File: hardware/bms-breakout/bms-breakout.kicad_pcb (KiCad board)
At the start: 2 copper layers, 116.5 x 125.3 mm, 32 parts, among them J1 IN-A, J10 V-SUPP, J11 Smol_Brain_Board, J13 UART_CONN, J16 ESTOP_CON, J17 I2C_Conn, J18 BAL_3, J19 BAL_2, J2 IN-B, J20 BAL_1, J21 DE9_Socket_MountingHoles, J22 DE9_Socket_MountingHoles, J23 FAN-IN, J24 SWITCH, J3 IN-C, J4 BALANCE-A, J5 BALANCE-B, J6 BALANCE-C, J7 Conn_01x02, Q1 PMOZZ, SW1 Kill_Switch

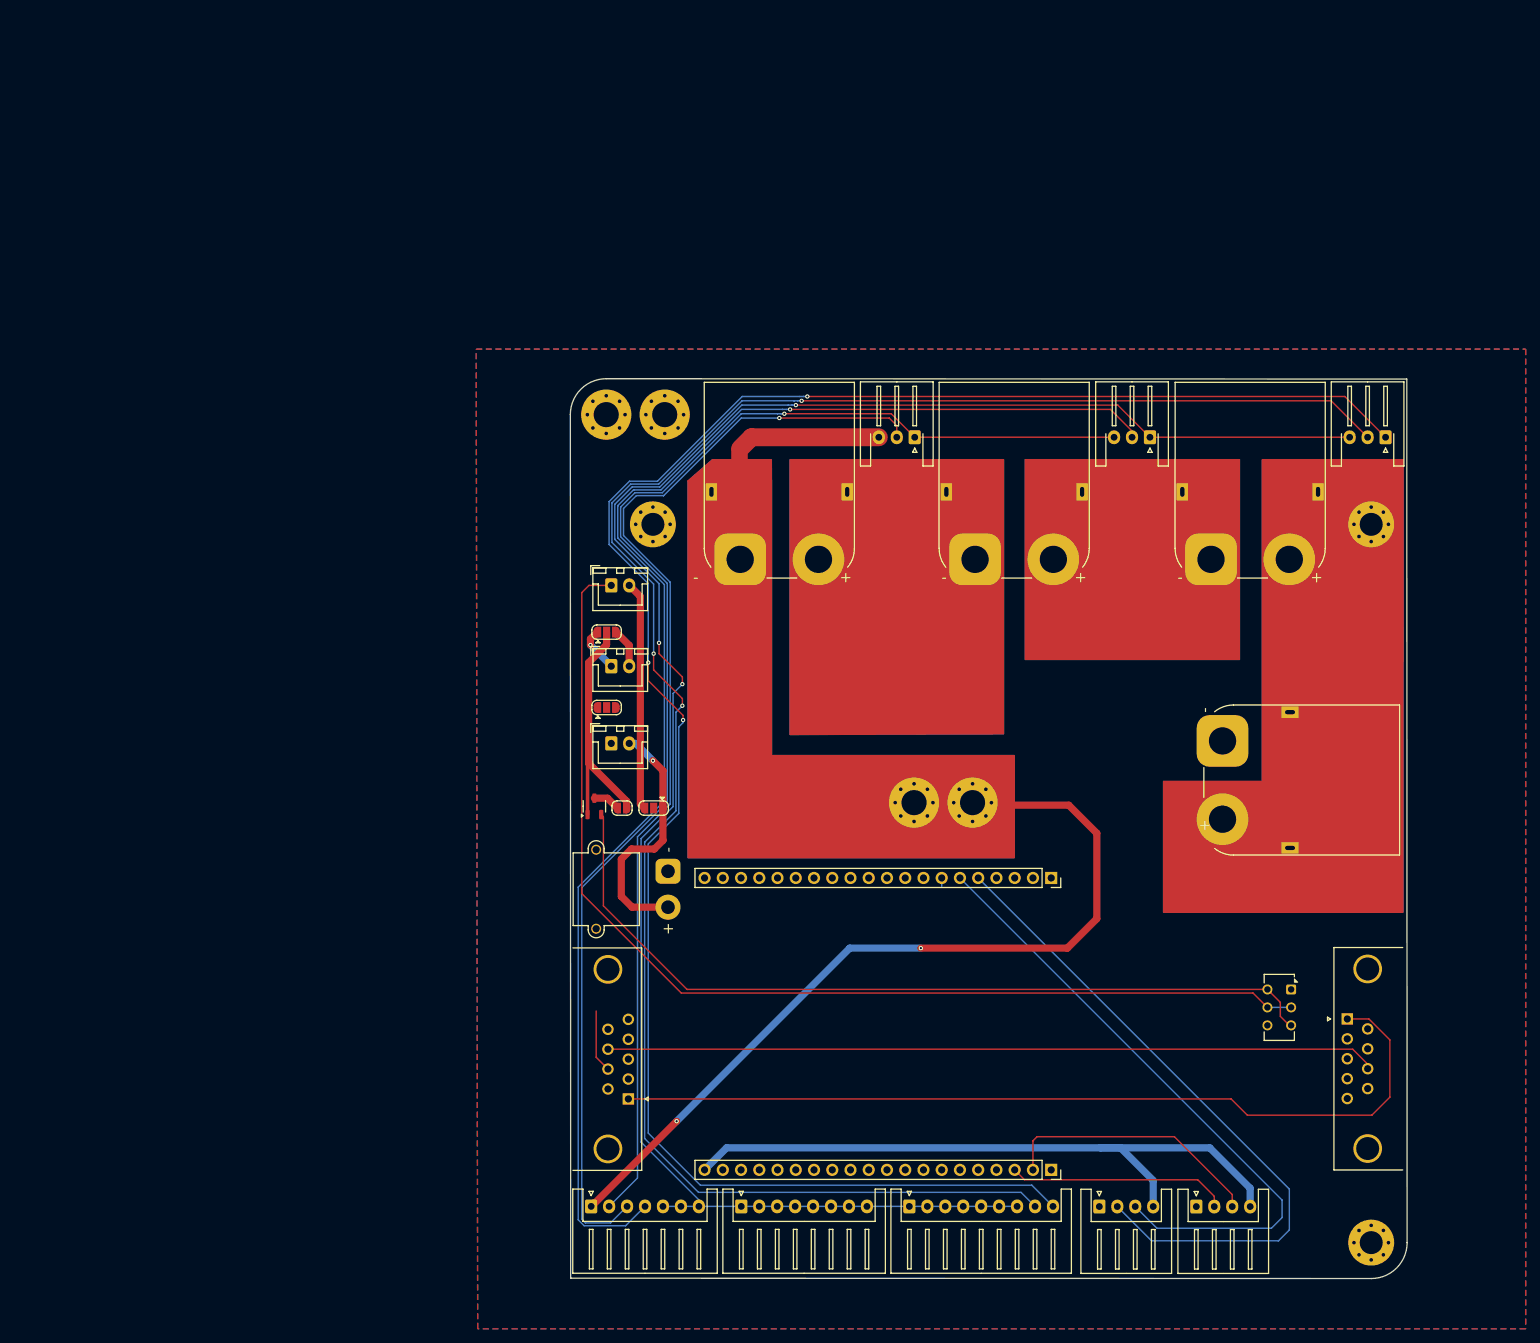
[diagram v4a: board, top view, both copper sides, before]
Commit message: Final Touches
- Added graphics
- Added text
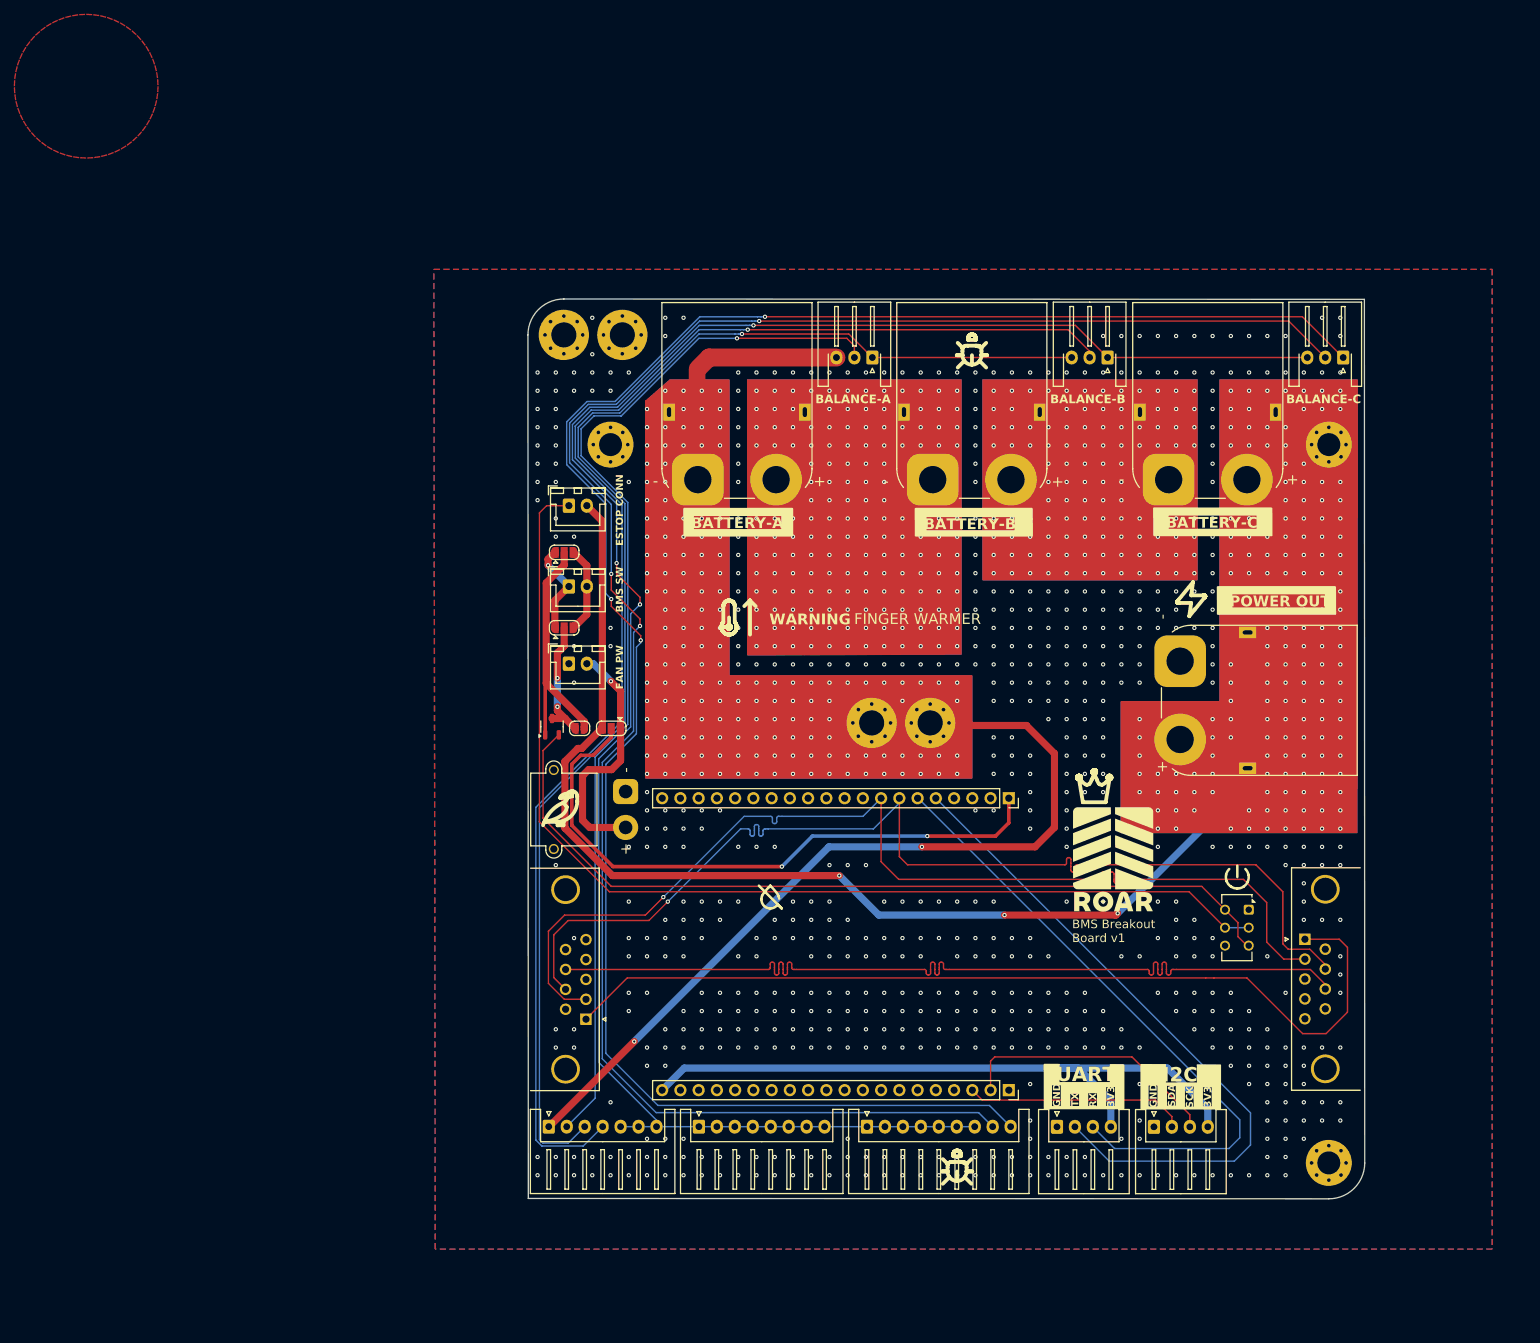
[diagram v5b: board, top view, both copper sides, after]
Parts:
- J1, J10, J2, J3: footprint Connector_AMASS:AMASS_XT90PW-M_1x02_P10.90mm_Horizontal -> custom-XT90:AMASS_XT90PW-M_1x02_P10.90mm_Horizontal
- moved J19 12.6 mm to (85.3, 144.9)
- moved J18 12.6 mm to (108.7, 144.9)
- moved J20 12.6 mm to (64.4, 144.9)
- moved J22 12.6 mm to (169.7, 118.8)
- moved Q1 12.6 mm to (64.8, 89.2)
- moved H1 12.6 mm to (73.0, 49.9)
- moved H3 12.6 mm to (173.0, 49.9)
- moved H5 12.6 mm to (66.5, 34.6)
- moved H6 12.6 mm to (74.6, 34.6)
- moved J2 12.6 mm to (117.8, 54.8)
- moved J3 12.6 mm to (150.7, 54.8)
- moved J5 12.6 mm to (142.2, 37.8)
- moved J6 12.6 mm to (175.0, 37.8)
- moved H2 12.6 mm to (173.0, 149.9)
- moved H7 12.6 mm to (109.4, 88.6)
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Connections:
- H3 pad 1: unconnected-(H3-Pad1)_1 -> VBUS
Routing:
- net VBUS: track 31.9 -> 184.1 mm, vias 0 -> 163
- net /CAN_L_A: track 0.00 -> 150.7 mm, vias 0 -> 1
- net /CAN_H_A: track 9.95 -> 150.8 mm, vias 0 -> 1
- net Net-(J11-VCC): track 0.00 -> 86.0 mm, vias 0 -> 2
- net /CAN_H_B: track 107.3 -> 127.9 mm
- net /MOZZ_S: track 3.77 -> 17.2 mm, vias 0 -> 2
- net /K_NEG: track 6.34 -> 12.9 mm
- net /K_POS: track 5.52 -> 12.0 mm
- net /CAN_L_B: track 123.1 -> 128.3 mm
- net Net-(Q1-G): track 116.6 -> 119.3 mm
- net /UART_TX: track 93.5 -> 94.6 mm
- net GND_B: track 137.9 -> 137.0 mm, vias 2 -> 157
- net Net-(J16-Pin_1): track 151.6 -> 152.3 mm
- net GND_C: vias 0 -> 608
- net /BAT2-3: vias 0 -> 108
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- added copper zone on F.Cu, net (none)
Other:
- outline, holes or cut-outs redrawn
- board text added: "3V3"
- board text added: "BALANCE-A"
- board text added: "BALANCE-B"
- board text added: "BALANCE-C"
- board text added: "BATTERY-A"
- board text added: "BATTERY-B"
- board text added: "BATTERY-C"
- board text added: "BMS Breakout Board v1"
- board text added: "BMS SW"
- board text added: "ESTOP CONN"
- board text added: "FAN PW"
- board text added: "FINGER WARMER"
- board text added: "GND"
- board text added: "I2C"
- board text added: "POWER OUT"
- board text added: "RX"
- board text added: "SCK"
- board text added: "SDA"
- board text added: "TX"
- board text added: "UART"
- board text added: "WARNING"

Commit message: Finished, ready for review
- Cleaned up traces
- Repositioned sw output
- Added edges
- Other finishes
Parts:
- JP4: footprint Jumper:SolderJumper-2_P1.3mm_Open_RoundedPad1.0x1.5mm -> Jumper:SolderJumper-2_P1.3mm_Bridged_RoundedPad1.0x1.5mm
- moved J24 125.0 mm to (163.0, 150.0)
- moved JP3 120.5 mm to (165.1, 144.8)
- moved JP2 118.5 mm to (164.4, 131.6)
- moved Q1 111.8 mm to (164.4, 140.2), turned to -90 degrees
- moved JP4 107.2 mm to (165.3, 135.8), turned to 90 degrees
- moved J16 13.0 mm to (67.2, 71.4)
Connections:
- JP3 pad 2: /MOZZ_S -> Net-(JP3-C)
- JP4 pad 1: /MOZZ_S -> /MOZZ_D
- Q1 pad 1: Net-(JP2-C) -> /MOZZ_D
- Q1 pad 3: /MOZZ_S -> Net-(JP3-C)
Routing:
- net Net-(Q1-G): track 119.3 -> 26.5 mm, vias 0 -> 1
- net Net-(JP2-C): track 34.9 -> 3.87 mm
- net /MOZZ_S: track 17.2 -> 0.00 mm, vias 2 -> 0
- net Net-(J16-Pin_1): track 152.3 -> 139.4 mm
- net VBUS: track 184.1 -> 174.2 mm
- net /K_POS: track 12.0 -> 20.2 mm
- net /K_NEG: track 12.9 -> 20.4 mm, vias 1 -> 0
- net Net-(JP3-C): track 0.00 -> 3.92 mm
- net /MOZZ_D: track 0.00 -> 2.63 mm
- net GND_C: vias 608 -> 617
- net GND_B: vias 157 -> 156
- net /BAT2-3: vias 108 -> 106
- net /BAT1-2: vias 157 -> 156
- removed copper zone on F.Cu, net (none)
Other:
- board text added: "VCC"

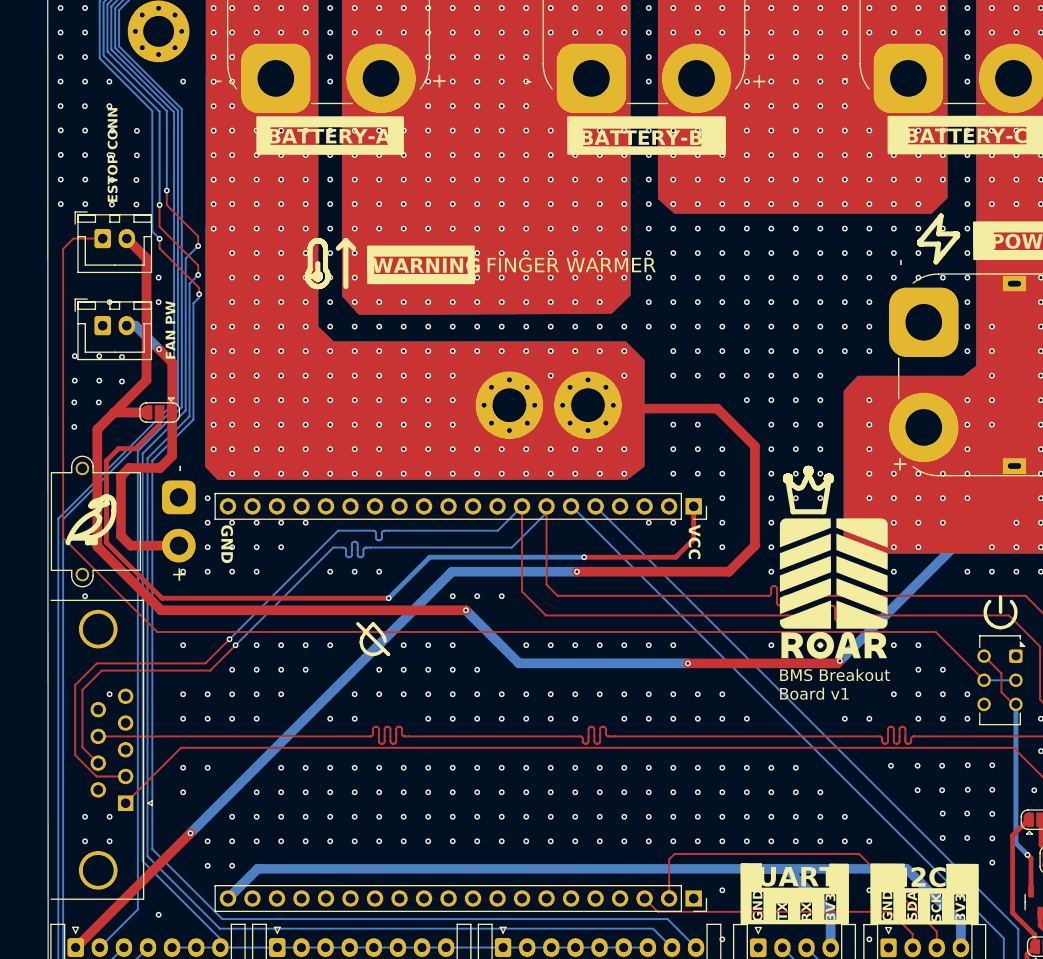
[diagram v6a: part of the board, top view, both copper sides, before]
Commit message: Redesigned switch off method
- Added NType MosFet for PWM for Fan
- Added voltage divider / pulldown resistor for mosfet control
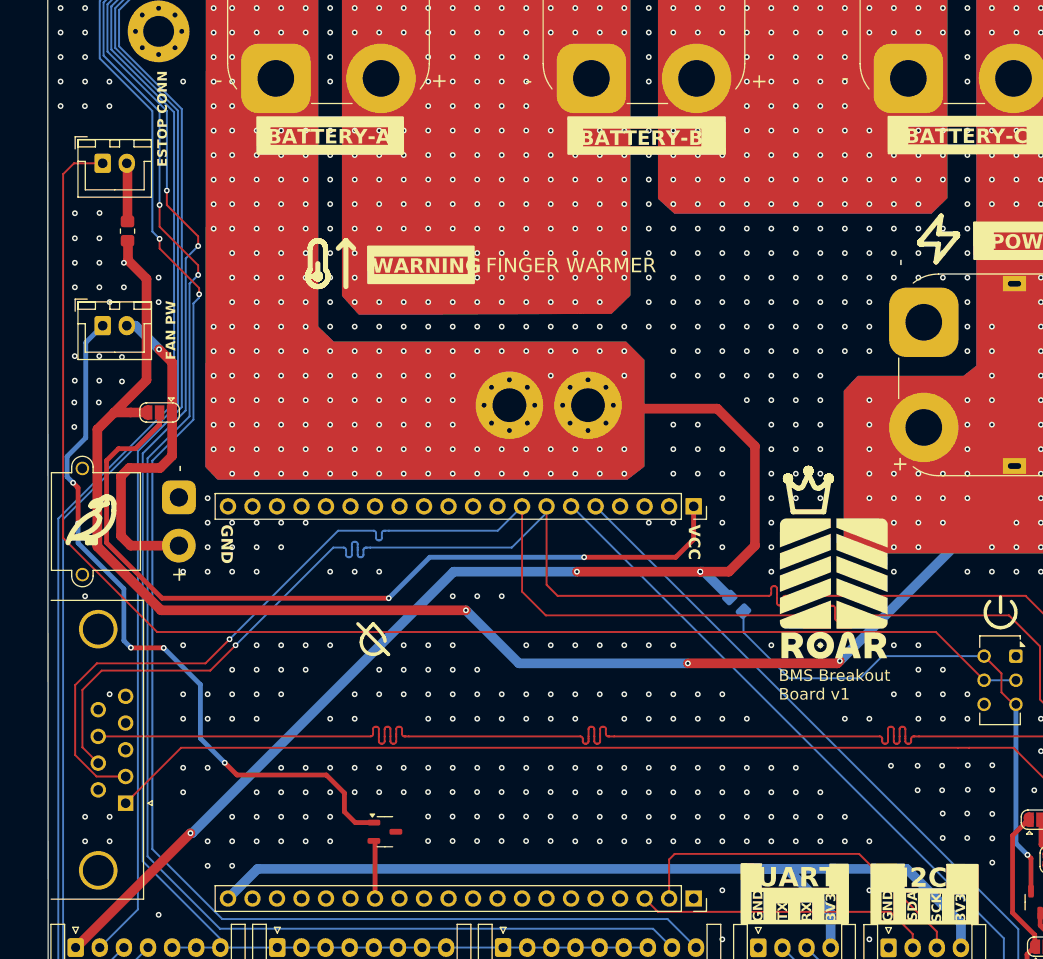
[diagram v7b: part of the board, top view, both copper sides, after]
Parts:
- added Q2: NMOS, Package_TO_SOT_SMD:SOT-23-3, F.Cu at (96.5, 132.8)
- added R2: 10k, Resistor_SMD:R_0805_2012Metric_Pad1.20x1.40mm_HandSolder, B.Cu at (132.9, 109.3)
- added R3: 10k, Resistor_SMD:R_0805_2012Metric_Pad1.20x1.40mm_HandSolder, F.Cu at (69.8, 70.6)
- moved J16 7.80 mm to (67.2, 63.6)
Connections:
- J11 pad 27: unconnected-(J11-IO45-Pad27) -> /FAN_PWM
- J16 pad 2: VBUS -> Net-(J16-Pin_2)
- J23 pad 1: GND_C -> Net-(J23-Pin_1)
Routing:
- net Net-(J23-Pin_1): track 0.00 -> 74.7 mm, vias 0 -> 5
- net Net-(Q1-G): track 26.5 -> 56.6 mm
- net Net-(J16-Pin_1): track 139.4 -> 147.1 mm
- net Net-(J16-Pin_2): track 0.00 -> 6.06 mm
- net /FAN_PWM: track 0.00 -> 6.02 mm
- net GND_B: track 137.0 -> 141.1 mm, vias 156 -> 158
- net GND_C: vias 617 -> 604
